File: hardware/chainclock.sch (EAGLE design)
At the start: 28 parts, among them IC1 TINY2313-*S*, Q1 IRLML2502, Q2 IRLML2502, Q3 IRLML2502, Q4 IRLML2502, Q6 BSS84, Y1 8MHz

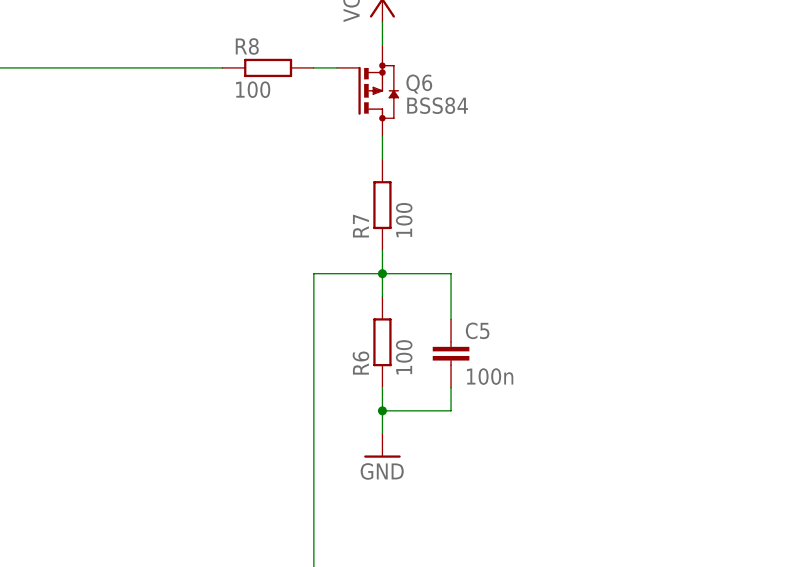
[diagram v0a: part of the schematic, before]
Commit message: voltage divider resistor values fixed
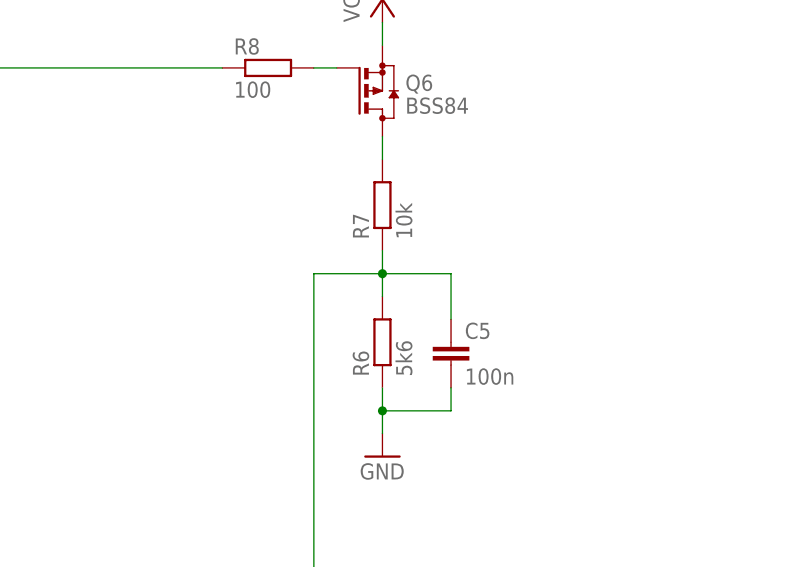
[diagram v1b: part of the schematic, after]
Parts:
- R6: value 100 -> 5k6
- R7: value 100 -> 10k
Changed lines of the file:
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@@
 <part name="R5" library="resistor" deviceset="R-EU_" device="R0603" value="10k"/>
 <part name="GND3" library="supply1" deviceset="GND" device=""/>
-<part name="R6" library="resistor" deviceset="R-EU_" device="R0603" value="100"/>
-<part name="R7" library="resistor" deviceset="R-EU_" device="R0603" value="100"/>
+<part name="R6" library="resistor" deviceset="R-EU_" device="R0603" value="5k6"/>
+<part name="R7" library="resistor" deviceset="R-EU_" device="R0603" value="10k"/>
 <part name="C5" library="rcl" deviceset="C-EU" device="C0603" value="100n"/>
 <part name="GND4" library="supply1" deviceset="GND" device=""/>
